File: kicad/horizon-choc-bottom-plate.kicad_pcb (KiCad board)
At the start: 2 copper layers, 252 x 68 mm, 68 parts, among them SW1 SW_Push, SW10 SW_Push, SW11 SW_Push, SW12 SW_Push, SW13 SW_Push, SW14 SW_Push, SW15 SW_Push, SW16 SW_Push, SW17 SW_Push, SW18 SW_Push, SW19 SW_Push, SW2 SW_Push, SW20 SW_Push, SW21 SW_Push, SW22 SW_Push, SW23 SW_Push, SW24 SW_Push, SW25 SW_Push, SW26 SW_Push, SW27 SW_Push, SW28 SW_Push, SW29 SW_Push, SW3 SW_Push, SW30 SW_Push, SW31 SW_Push, SW32 SW_Push, SW33 SW_Push, SW34 SW_Push, SW35 SW_Push, SW36 SW_Push, SW37 SW_Push, SW38 SW_Push, SW39 SW_Push, SW4 SW_Push, SW40 SW_Push, SW41 SW_Push, SW42 SW_Push, SW43 SW_Push, SW44 SW_Push, SW45 SW_Push, SW46 SW_Push, SW47 SW_Push, SW48 SW_Push, SW49 SW_Push, SW5 SW_Push, SW50 SW_Push, SW51 SW_Push, SW52 SW_Push, SW6 SW_Push, SW7 SW_Push, SW8 SW_Push, SW9 SW_Push, U1 PRO-MICRO

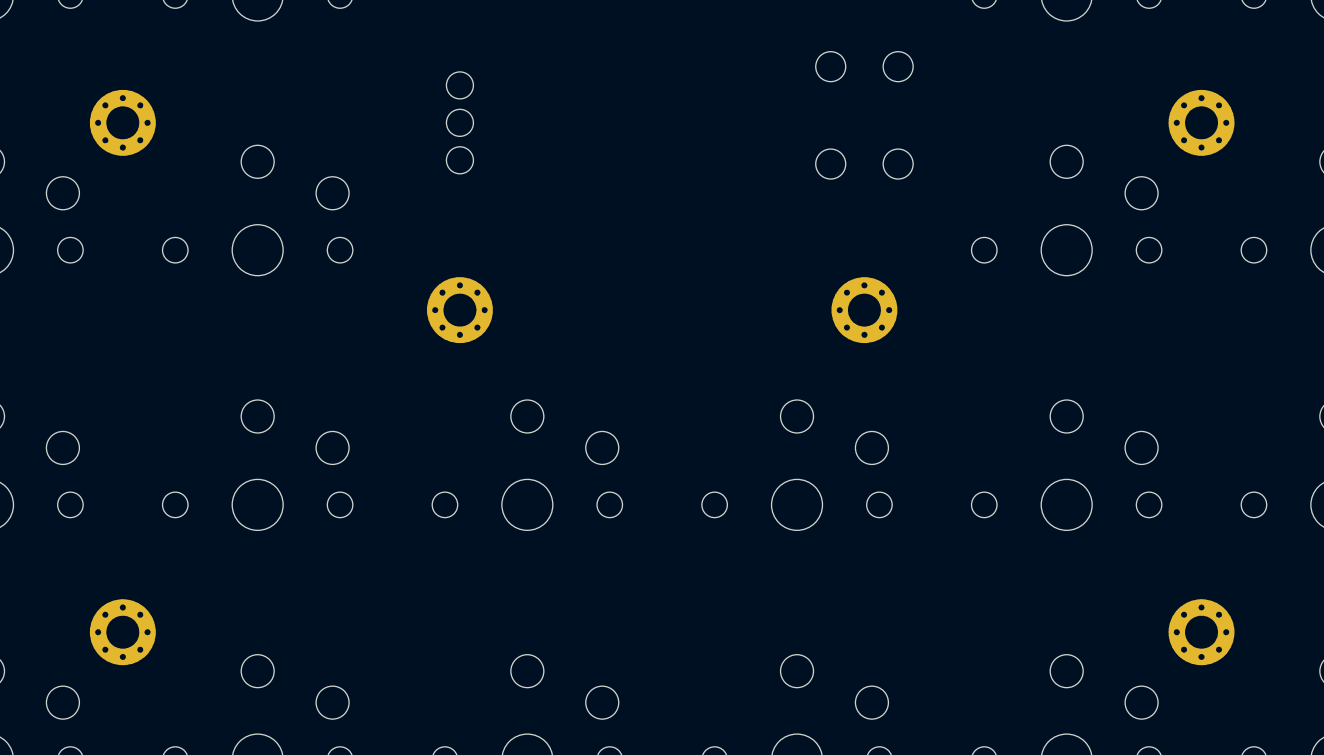
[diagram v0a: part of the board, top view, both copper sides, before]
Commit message: Use 50-key layout
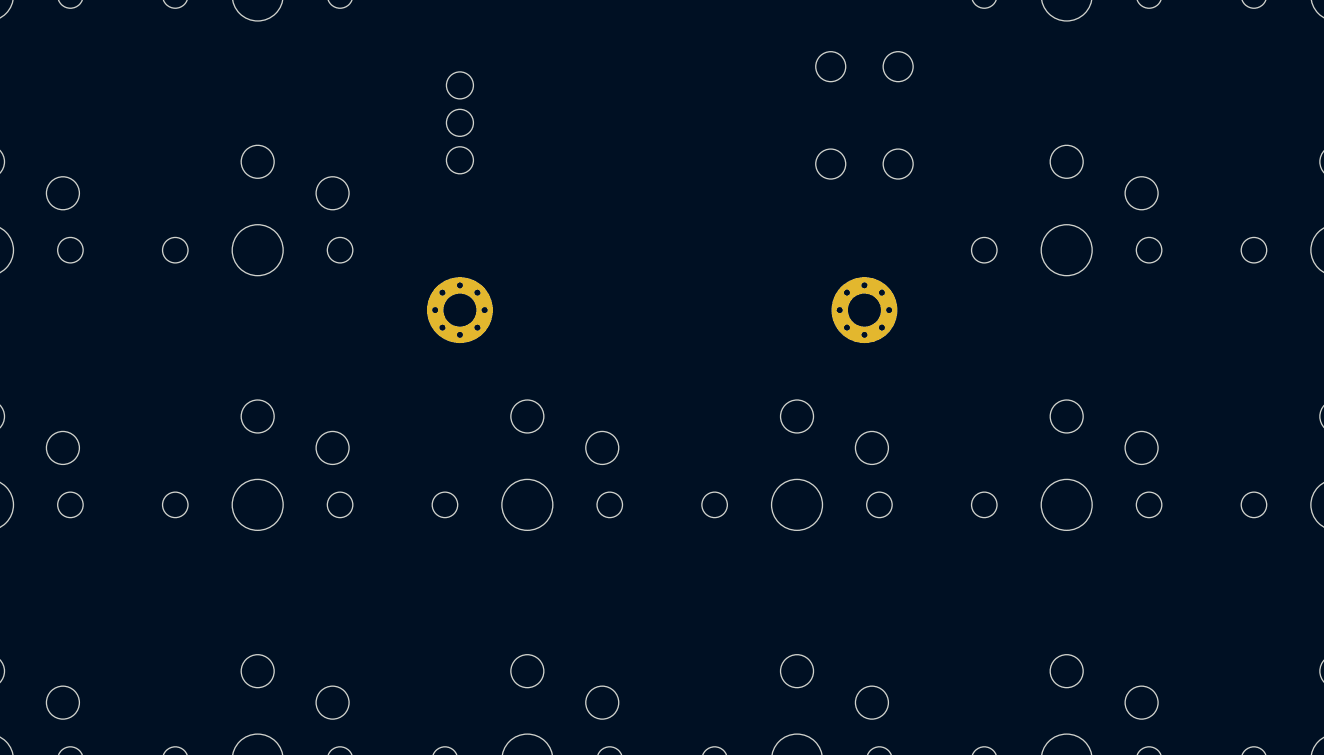
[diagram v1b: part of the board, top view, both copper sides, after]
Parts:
- removed H2, H3, H6, H7: Hole_Pad, horizon-footprints:Mount_M2

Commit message: Layout MX PCB
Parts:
- removed H9: Hole_Pad, horizon-footprints:Mount_M2
- removed W1: BATTERY, horizon-footprints:Cutout-Battery_Wire_Pads
- added ?: Hole_Pad, horizon-footprints:Mount_M2, F.Cu at (188.5, 99.5)
- added TB1: BATTERY, horizon-footprints:Cutout-KF350-2P, F.Cu at (215.5, 112.0)
- moved BTN1 27.2 mm to (188.5, 115.0), turned to 270 degrees
- moved SS1 4.00 mm to (188.5, 108.0), turned to 0 degrees
- renumbered H12 to ?, H11 to ?, H10 to ?
